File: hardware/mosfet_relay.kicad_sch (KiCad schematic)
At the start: 4 parts, among them Q1 AO3400A

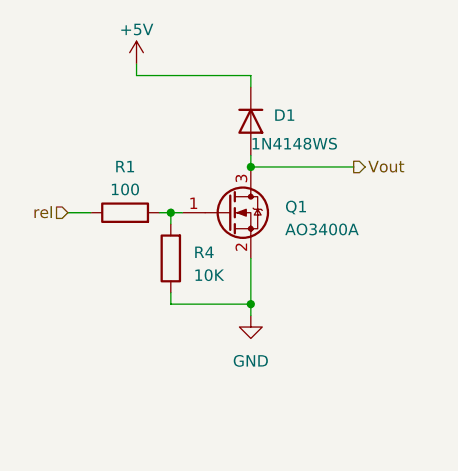
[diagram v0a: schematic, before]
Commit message: capacitor at mosfet
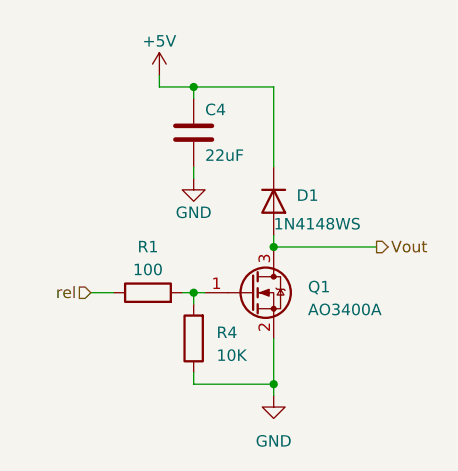
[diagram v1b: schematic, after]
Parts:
- added C4: 22uF, Capacitor_SMD:C_0805_2012Metric, symbol Device:C
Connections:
- net +5V: now also C4.1
- net GND: now also C4.2
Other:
- moved on the sheet: D1, Q1, R1, R4

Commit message: fix JLCPCB Part #
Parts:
- C4: JLCPCB Part # C96123 -> C45783
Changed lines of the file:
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@@
       (effects (font (size 1.27 1.27)) hide)
     )
-    (property "JLCPCB Part #" "C96123" (at 43.18 30.48 0)
+    (property "JLCPCB Part #" "C45783" (at 43.18 30.48 0)
       (effects (font (size 1.27 1.27)) hide)
     )
